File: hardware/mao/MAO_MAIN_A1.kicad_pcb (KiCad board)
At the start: 4 copper layers, 58 x 56 mm, 137 parts, among them J101 USB-C, J102 BAT, J201 TAG, J301 LCD, J501 LRA, Q101 AO3401A, Q302 DMG2302UK, Q501 AO3400A, SW301 SKQGADE010, U101 TPD2E2U06, U102 BQ25185DLHR, U103 MAX17048G+T10, U104 TPS62840DLCR, U105 TPS22916CYFPR, U201 ESP32-S3-MINI-1-N8, U301 DRV5012AEDMRR, U302 DRV5012AEDMRR, U304 TLV9061IDBVR, U401 ICM-42670-P, U402 VL53L4CDV0DH/1, U501 MAX98357AETE+T, U502 DRV2605LDGSR, U503 IRM-H638T/TR2, U504 TPS22916CYFPR

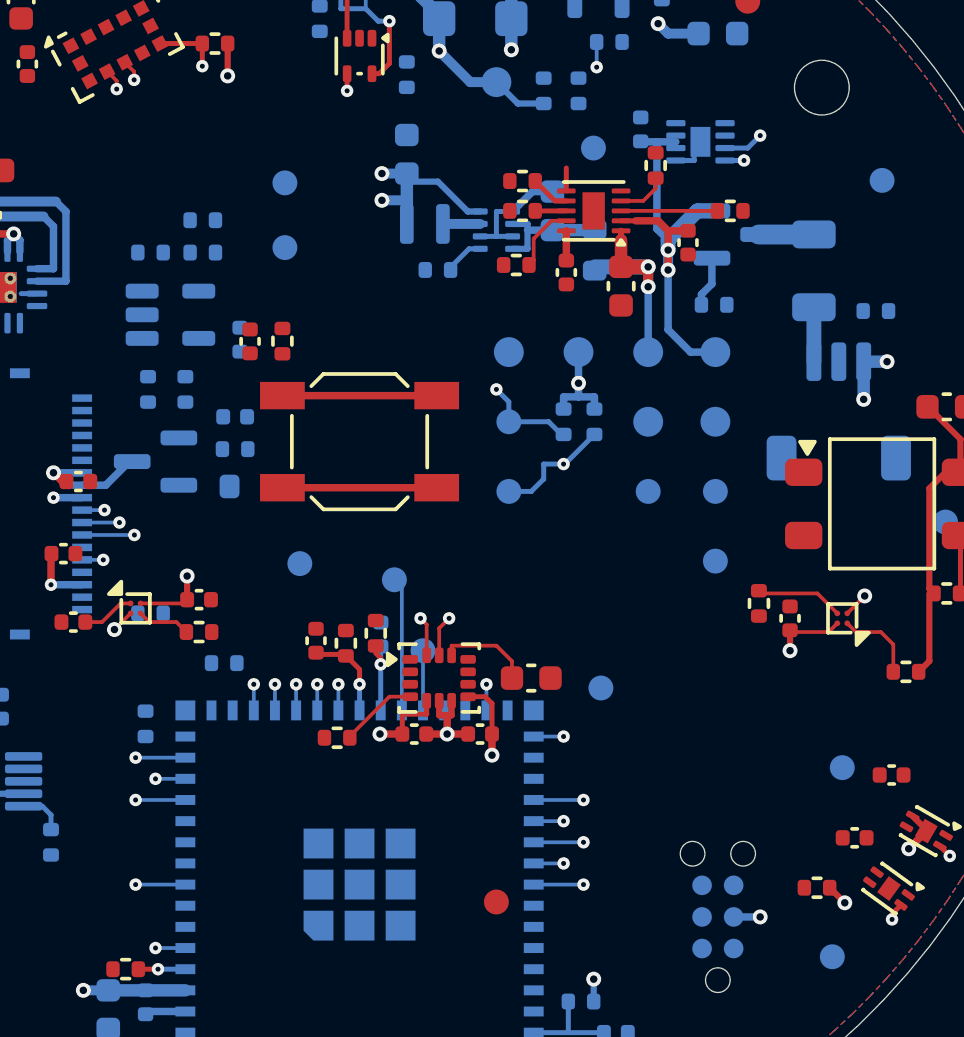
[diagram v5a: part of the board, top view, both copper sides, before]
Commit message: A1 layout: hand-designed VBUS/STAT1/NTC/BOOT/LCD_PWR_EN links, router sees the tail slot, I2S allowed on L3
Co-Authored-By: Claude Opus 5.5 <noreply@anthropic.com>
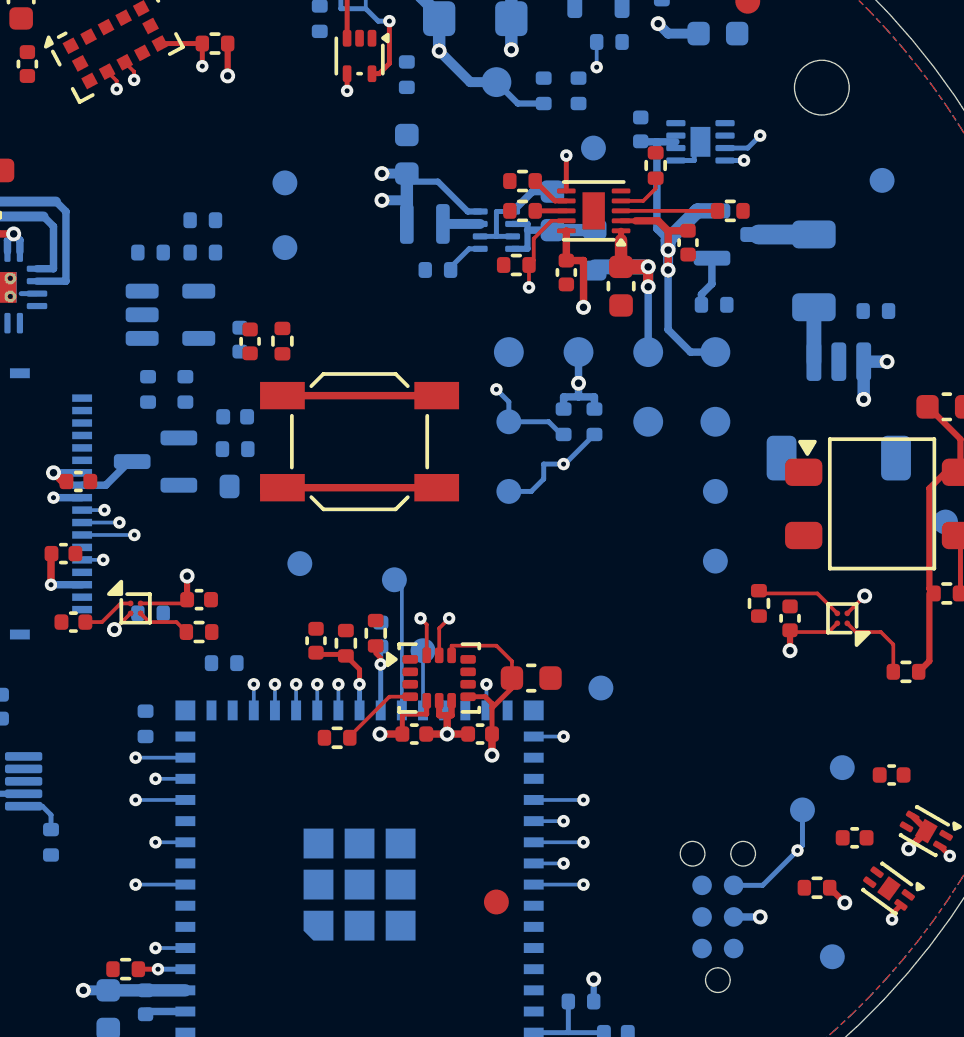
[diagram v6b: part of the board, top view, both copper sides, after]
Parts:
- moved TP8 14.2 mm to (67.8, 62.3)
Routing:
- net BOOT: track 1.89 -> 40.4 mm, vias 1 -> 2
- net VBUS: track 10.9 -> 24.5 mm, vias 2 -> 3
- net +3V3: track 34.3 -> 35.8 mm
- net LCD_PWR_EN: track 2.15 -> 3.35 mm, vias 0 -> 1
- net CHG_STAT1: track 2.74 -> 3.64 mm, vias 0 -> 1
- net BAT_NTC: track 0.92 -> 1.42 mm, vias 0 -> 1

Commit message: A1 capture/layout follow the pin swaps (ERC 0); escapes and fixture pads moved with their nets
Co-Authored-By: Claude Opus 5.5 <noreply@anthropic.com>
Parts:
- TP24: value IO21 -> IO2
- moved TP21 19.5 mm to (51.4, 53.0)
- moved TP24 18.1 mm to (39.8, 67.0)
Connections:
- TP24 pad 1: GPIO21 -> GPIO2
- U201 pad 18: HAPTIC_EN -> PRESS_N
- U201 pad 20: AUX_PWR_EN -> TOF_INT_N
- U201 pad 25: GPIO21 -> HALL_A
- U201 pad 34: TOF_INT_N -> AUX_PWR_EN
- U201 pad 5: PRESS_N -> HAPTIC_EN
- U201 pad 6: HALL_A -> GPIO2
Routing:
- net HALL_A: track 0.00 -> 5.37 mm
- net GPIO21: track 5.37 -> 0.00 mm
- net GPIO2: track 0.00 -> 3.20 mm
- net TOF_INT_N: track 4.61 -> 3.66 mm
- net AUX_PWR_EN: track 4.53 -> 5.48 mm

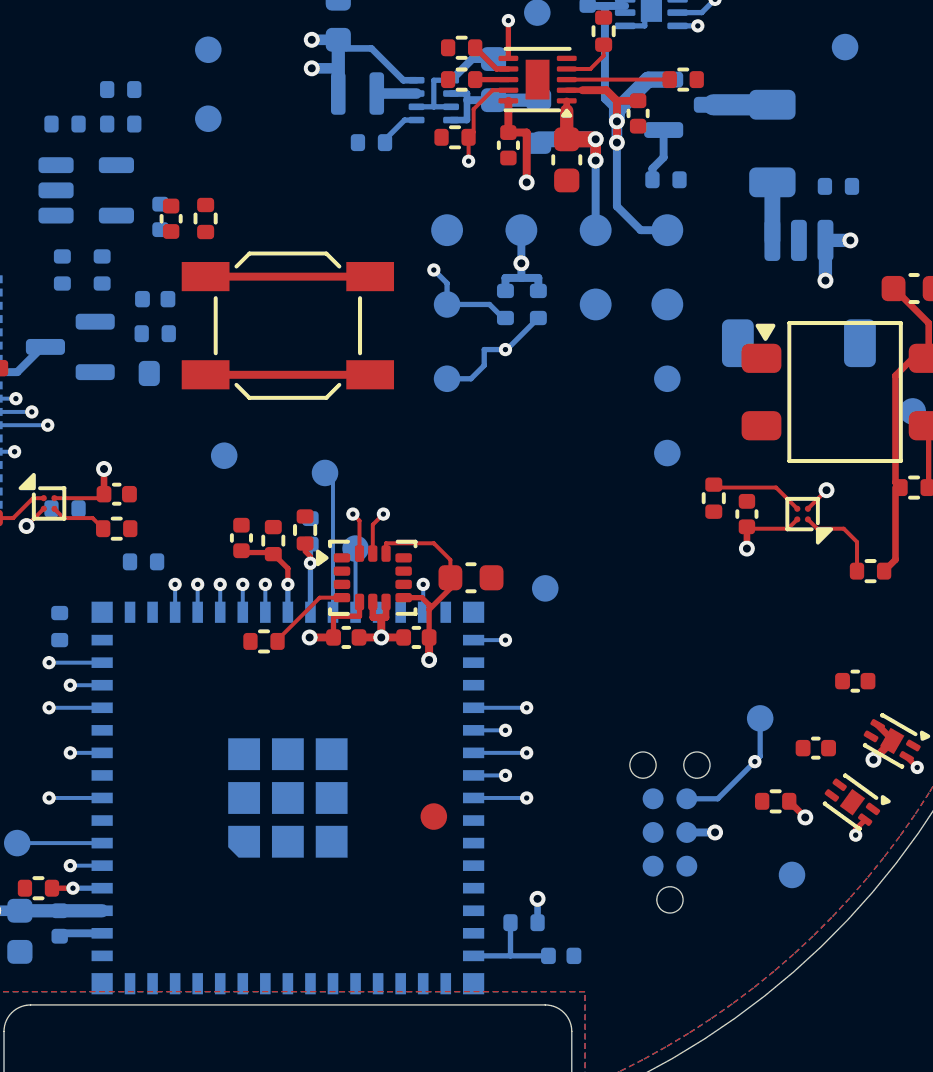
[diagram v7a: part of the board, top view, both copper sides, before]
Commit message: A1 layout: Tag-Connect turned for UART order, designed UART/BOOT/PRESS/STAT1 runs
Co-Authored-By: Claude Opus 5.5 <noreply@anthropic.com>
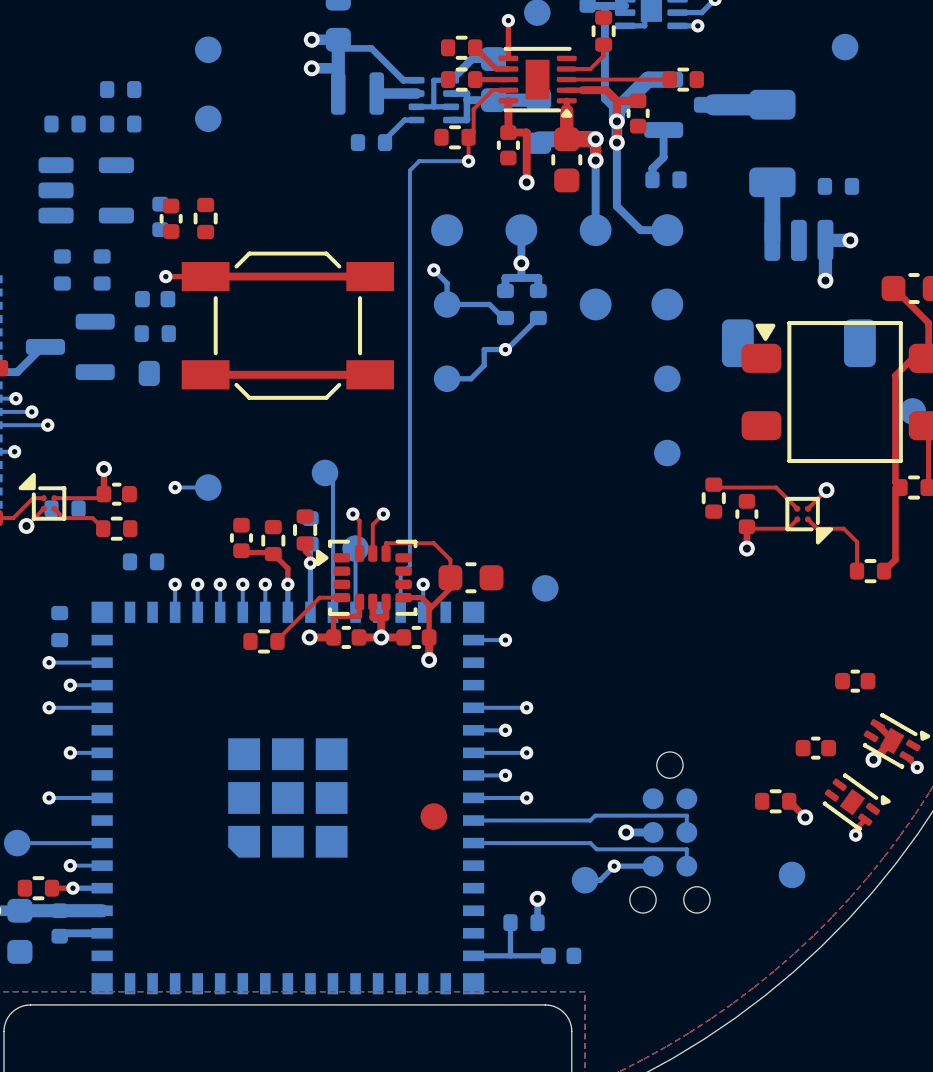
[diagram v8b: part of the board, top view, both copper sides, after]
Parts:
- moved TP8 8.99 mm to (61.2, 68.4)
- moved TP20 1.34 mm to (47.0, 53.6)
- turned J201 to -90 degrees
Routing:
- net CHG_STAT1: track 3.64 -> 22.8 mm
- net PRESS_N: track 7.25 -> 21.7 mm, vias 1 -> 3
- net BOOT: track 40.4 -> 29.3 mm
- net UART_RX: track 0.00 -> 8.77 mm
- net UART_TX: track 0.00 -> 8.75 mm
